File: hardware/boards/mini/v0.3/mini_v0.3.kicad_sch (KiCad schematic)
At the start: 95 parts, among them IC1 NAU88C22YG, IC3 IS42S16160J-6BLI, J2 Top (A), J3 Bottom (B), U1 W25Q128JVP, U2 LTV-217-G, U4 STM32H750XBHx, Y1 Crystal_GND24, Y3 32.768kHz

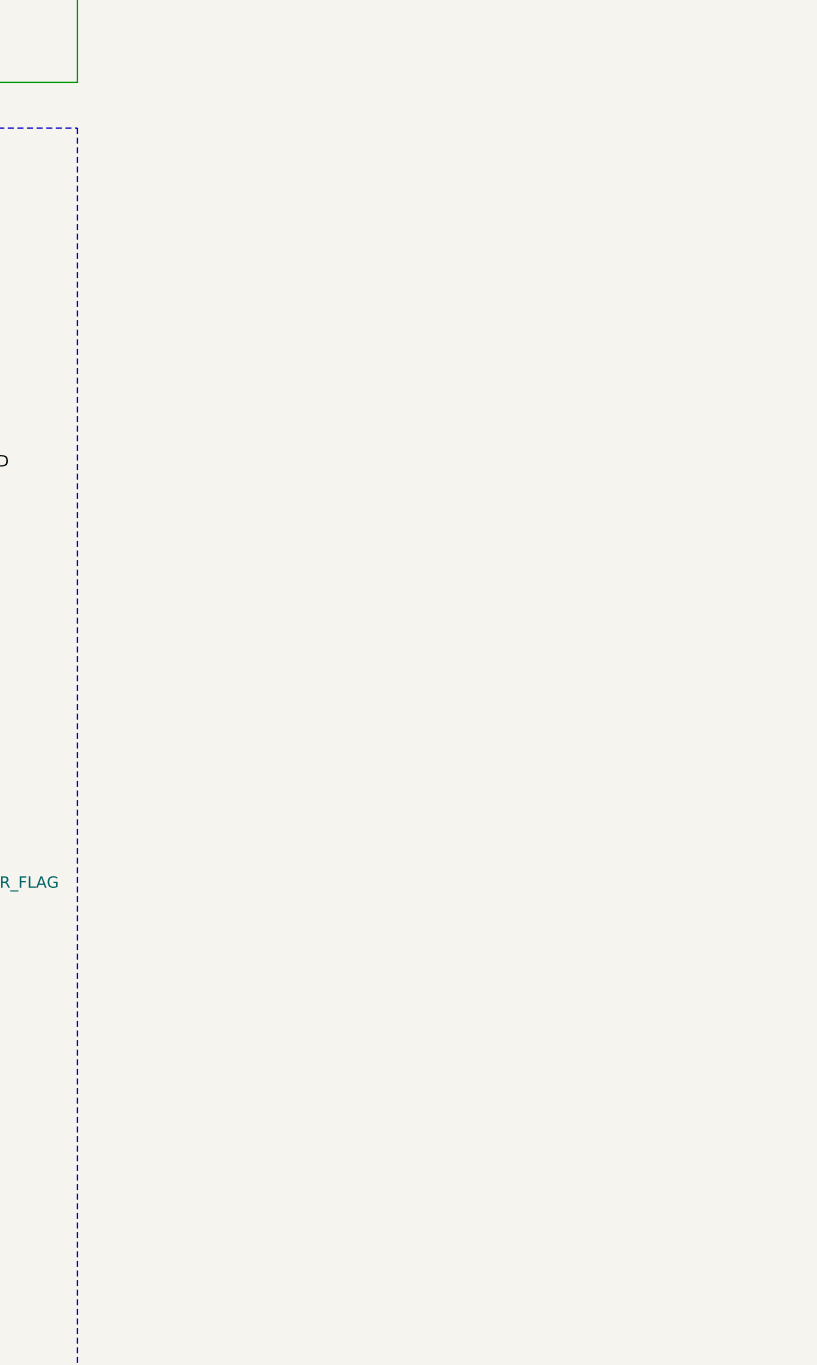
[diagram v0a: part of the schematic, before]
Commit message: mini: start routing single connector layout
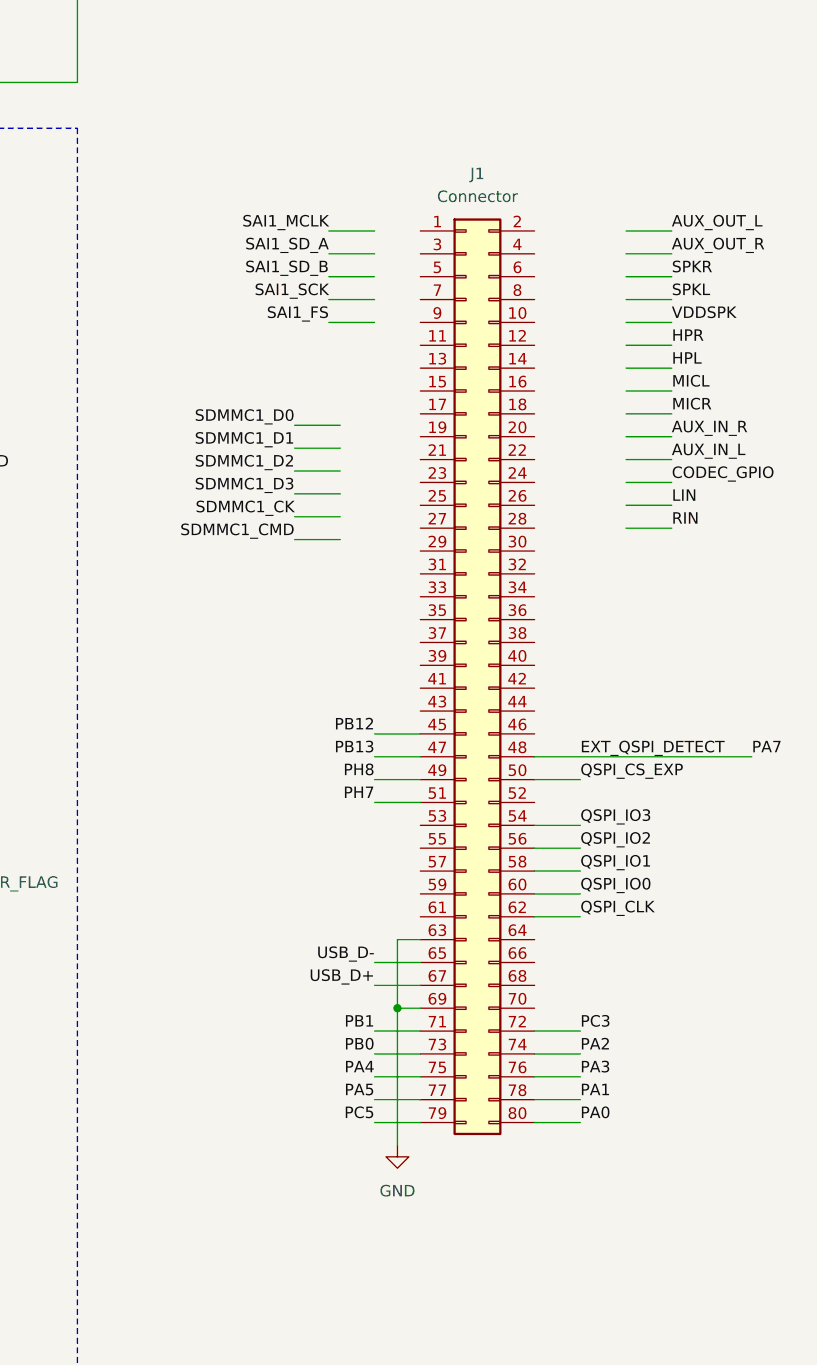
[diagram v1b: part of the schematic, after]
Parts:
- added J1: Connector, Connector_Hirose_DF40:Hirose_DF40C-80DP-0.4V_2x40-1MP_P0.4mm, symbol Connector_Generic:Conn_02x40_Odd_Even
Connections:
- net PA7 is gone; now on net EXT_QSPI_DETECT: J3.37, U4.R5 (PA7)
- net EXT_QSPI_DETECT: now also J1.48 (Pin_48)
- net GND: now also J1.63 (Pin_63), J1.69 (Pin_69)
- net PA0: now also J1.80 (Pin_80)
- net PA1: now also J1.78 (Pin_78)
- net PA2: now also J1.74 (Pin_74)
- net PA3: now also J1.76 (Pin_76)
- net PA4: now also J1.75 (Pin_75)
- net PA5: now also J1.77 (Pin_77)
- net PB0: now also J1.73 (Pin_73)
- net PB1: now also J1.71 (Pin_71)
- net PB12: now also J1.45 (Pin_45)
- net PB13: now also J1.47 (Pin_47)
- net PC3: now also J1.72 (Pin_72)
- net PC5: now also J1.79 (Pin_79)
- net PH7: now also J1.51 (Pin_51)
- net PH8: now also J1.49 (Pin_49)
- net QSPI_CLK: now also J1.62 (Pin_62)
- net QSPI_CS_EXP: now also J1.50 (Pin_50)
- net QSPI_IO0: now also J1.60 (Pin_60)
- net QSPI_IO1: now also J1.58 (Pin_58)
- net QSPI_IO2: now also J1.56 (Pin_56)
- net QSPI_IO3: now also J1.54 (Pin_54)
- net USB_D+: now also J1.67 (Pin_67)
- net USB_D-: now also J1.65 (Pin_65)

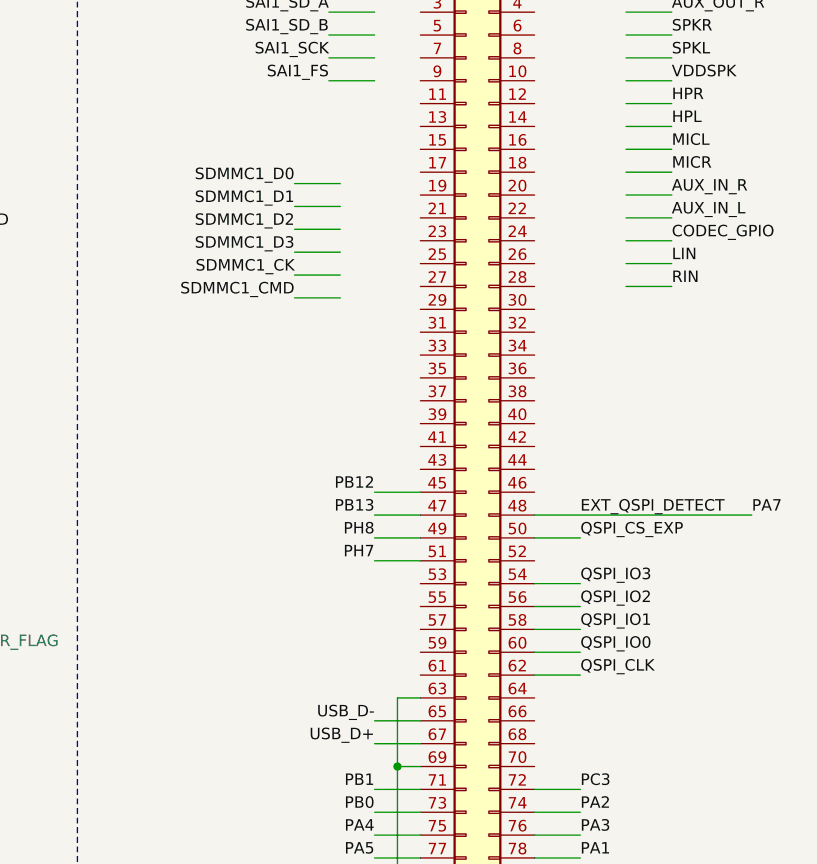
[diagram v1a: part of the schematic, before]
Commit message: mini: route SDMMC and SAI lines to near new connector
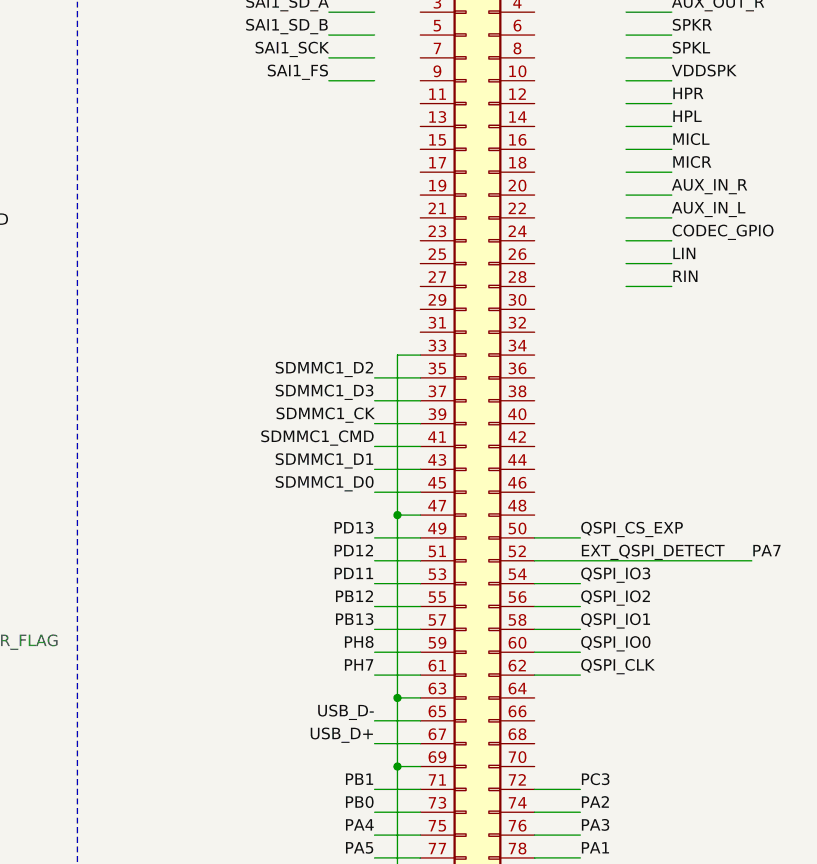
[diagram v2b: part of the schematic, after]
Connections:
- net EXT_QSPI_DETECT: now also J1.52 (Pin_52); no longer J1.48 (Pin_48)
- net GND: now also J1.33 (Pin_33), J1.47 (Pin_47)
- net PB12: now also J1.55 (Pin_55); no longer J1.45 (Pin_45)
- net PB13: now also J1.57 (Pin_57); no longer J1.47 (Pin_47)
- net PD11: now also J1.53 (Pin_53)
- net PD12: now also J1.51 (Pin_51)
- net PD13: now also J1.49 (Pin_49)
- net PH7: now also J1.61 (Pin_61); no longer J1.51 (Pin_51)
- net PH8: now also J1.59 (Pin_59); no longer J1.49 (Pin_49)
- net SDMMC1_CK: now also J1.39 (Pin_39)
- net SDMMC1_CMD: now also J1.41 (Pin_41)
- net SDMMC1_D0: now also J1.45 (Pin_45)
- net SDMMC1_D1: now also J1.43 (Pin_43)
- net SDMMC1_D2: now also J1.35 (Pin_35)
- net SDMMC1_D3: now also J1.37 (Pin_37)
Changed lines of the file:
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@@
 	)
 	(junction
+		(at 439.42 139.7)
+		(diameter 0)
+		(color 0 0 0 0)
+	)
+	(junction
 		(at 195.58 22.86)
 		(diameter 0)
@@
 	)
 	(junction
+		(at 439.42 119.38)
+		(diameter 0)
+		(color 0 0 0 0)
+	)
+	(junction
 		(at 278.13 238.76)
 		(diameter 0)
@@
 	(wire
 		(pts
+			(xy 441.96 101.6) (xy 439.42 101.6)
+		)
+		(stroke
+			(width 0)
+			(type default)
+		)
+	)
+	(wire
+		(pts
 			(xy 167.64 58.42) (xy 170.18 58.42)
 		)
@@
 	(wire
 		(pts
+			(xy 439.42 119.38) (xy 439.42 139.7)
+		)
+		(stroke
+			(width 0)
+			(type default)
+		)
+	)
+	(wire
+		(pts
 			(xy 134.62 22.86) (xy 134.62 26.67)
 		)
@@
 	(wire
 		(pts
-			(xy 427.99 85.09) (xy 433.07 85.09)
+			(xy 436.88 106.68) (xy 441.96 106.68)
 		)
 		(stroke
@@
 	(wire
 		(pts
+			(xy 441.96 124.46) (xy 436.88 124.46)
+		)
+		(stroke
+			(width 0)
+			(type default)
+		)
+	)
+	(wire
+		(pts
 			(xy 45.72 74.93) (xy 48.26 74.93)
 		)
@@
 	(wire
 		(pts
-			(xy 427.99 92.71) (xy 433.07 92.71)
+			(xy 436.88 114.3) (xy 441.96 114.3)
 		)
 		(stroke
@@
 	(wire
 		(pts
-			(xy 436.88 116.84) (xy 441.96 116.84)
+			(xy 436.88 129.54) (xy 441.96 129.54)
 		)
 		(stroke
@@
 	(wire
 		(pts
+			(xy 441.96 127) (xy 436.88 127)
+		)
+		(stroke
+			(width 0)
+			(type default)
+		)
+	)
+	(wire
+		(pts
 			(xy 212.09 168.91) (xy 214.63 168.91)
 		)
@@
 	(wire
 		(pts
-			(xy 436.88 124.46) (xy 441.96 124.46)
+			(xy 436.88 137.16) (xy 441.96 137.16)
 		)
 		(stroke
@@
 	(wire
 		(pts
+			(xy 439.42 101.6) (xy 439.42 119.38)
+		)
+		(stroke
+			(width 0)
+			(type default)
+		)
+	)
+	(wire
+		(pts
 			(xy 266.7 91.44) (xy 262.89 91.44)
 		)
@@
 	(wire
 		(pts
-			(xy 427.99 82.55) (xy 433.07 82.55)
+			(xy 436.88 104.14) (xy 441.96 104.14)
 		)
 		(stroke
@@
 	(wire
 		(pts
-			(xy 436.88 119.38) (xy 441.96 119.38)
+			(xy 436.88 132.08) (xy 441.96 132.08)
 		)
 		(stroke
@@
 	(wire
 		(pts
-			(xy 427.99 95.25) (xy 433.07 95.25)
+			(xy 436.88 116.84) (xy 441.96 116.84)
 		)
 		(stroke
@@
 	(wire
 		(pts
-			(xy 427.99 90.17) (xy 433.07 90.17)
+			(xy 436.88 111.76) (xy 441.96 111.76)
 		)
 		(stroke
@@
 	(wire
 		(pts
+			(xy 441.96 121.92) (xy 436.88 121.92)
+		)
+		(stroke
+			(width 0)
+			(type default)
+		)
+	)
+	(wire
+		(pts
 			(xy 353.06 238.76) (xy 353.06 203.2)
 		)
@@
 	(wire
 		(pts
-			(xy 454.66 119.38) (xy 478.79 119.38)
+			(xy 454.66 124.46) (xy 478.79 124.46)
 		)
 		(stroke
@@
 	(wire
 		(pts
+			(xy 441.96 119.38) (xy 439.42 119.38)
+		)
+		(stroke
+			(width 0)
+			(type default)
+		)
+	)
+	(wire
+		(pts
 			(xy 45.72 110.49) (xy 48.26 110.49)
 		)
@@
 	(wire
 		(pts
-			(xy 433.07 87.63) (xy 427.99 87.63)
+			(xy 441.96 109.22) (xy 436.88 109.22)
 		)
 		(stroke
@@
 	(wire
 		(pts
-			(xy 436.88 121.92) (xy 441.96 121.92)
+			(xy 436.88 134.62) (xy 441.96 134.62)
 		)
 		(stroke
@@
 	)
 	(label "SDMMC1_D0"
-		(at 427.99 82.55 180)
+		(at 436.88 116.84 180)
 		(effects
 			(font
@@
 	)
 	(label "SDMMC1_D1"
-		(at 427.99 85.09 180)
+		(at 436.88 114.3 180)
 		(effects
 			(font
@@
 	)
 	(label "PB12"
-		(at 436.88 116.84 180)
+		(at 436.88 129.54 180)
 		(effects
 			(font
@@
 	)
 	(label "PB13"
-		(at 436.88 119.38 180)
+		(at 436.88 132.08 180)
 		(effects
 			(font
@@
 	)
 	(label "EXT_QSPI_DETECT"
-		(at 459.74 119.38 0)
+		(at 459.74 124.46 0)
 		(effects
 			(font
@@
 	)
 	(label "SDMMC1_CK"
-		(at 427.99 92.71 180)
+		(at 436.88 109.22 180)
 		(effects
 			(font
@@
 	)
 	(label "PH8"
-		(at 436.88 121.92 180)
+		(at 436.88 134.62 180)
 		(effects
 			(font
@@
 	)
 	(label "SDMMC1_D2"
-		(at 427.99 87.63 180)
+		(at 436.88 104.14 180)
 		(effects
 			(font
@@
 	)
 	(label "PA7"
-		(at 478.79 119.38 0)
+		(at 478.79 124.46 0)
 		(effects
 			(font
@@
 	)
 	(label "PH7"
-		(at 436.88 124.46 180)
+		(at 436.88 137.16 180)
 		(effects
 			(font
@@
 		)
 	)
+	(label "PD11"
+		(at 436.88 127 180)
+		(effects
+			(font
+				(size 1.27 1.27)
+			)
+			(justify right bottom)
+		)
+	)
 	(label "PA7"
 		(at 48.26 41.91 0)
@@
 	)
 	(label "SDMMC1_CMD"
-		(at 427.99 95.25 180)
+		(at 436.88 111.76 180)
 		(effects
 			(font
@@
 		)
 	)
+	(label "PD13"
+		(at 436.88 121.92 180)
+		(effects
+			(font
+				(size 1.27 1.27)
+			)
+			(justify right bottom)
+		)
+	)
 	(label "SWD_IO"
 		(at 48.26 57.15 0)
@@
 		)
 	)
+	(label "PD12"
+		(at 436.88 124.46 180)
+		(effects
+			(font
+				(size 1.27 1.27)
+			)
+			(justify right bottom)
+		)
+	)
 	(label "PA3"
 		(at 48.26 31.75 0)
@@
 	)
 	(label "SDMMC1_D3"
-		(at 427.99 90.17 180)
+		(at 436.88 106.68 180)
 		(effects
 			(font
